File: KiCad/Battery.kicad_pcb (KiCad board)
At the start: 2 copper layers, 19 x 29 mm, 25 parts, among them J1 Connector, J2 USB-C, J3 DC, Q1 RN1701, Q2 BSS169, Q3 BSS169, U1 ESP32-WROOM-32, U2 FT231XQ

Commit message: Tidy up PCB
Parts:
- added D2: D, Diode_SMD:D_1206_3216Metric, F.Cu at (131.7, 115.4)
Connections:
- R5 pad 1: VBUS -> DC
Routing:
- net DC: track 40.7 -> 62.6 mm, vias 3 -> 4
- net VBUS: track 51.2 -> 37.0 mm
- net USB3.3: track 14.5 -> 16.0 mm
- net GND: track 148.1 -> 149.0 mm
- net IO1: track 10.1 -> 9.59 mm
- net Net-(Q2-Pad1): track 15.6 -> 15.1 mm
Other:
- board text added: "2021-05-22"
- board text added: "V2"
- board text removed: "2021-05-20"
- board text removed: "V3"

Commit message: Library update
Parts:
- removed Q2: BSS169, Package_TO_SOT_SMD:SOT-23
- removed R10: 10K, RevK:R_0603
- Q3: value BSS169 -> 2N7002
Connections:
- U1 pad 35: Net-(Q2-Pad1) -> O
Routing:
- net Net-(Q2-Pad1): track 15.1 -> 0.00 mm, vias 1 -> 0
- net O: track 9.10 -> 21.5 mm, vias 0 -> 1
- net VBUS: track 37.0 -> 34.0 mm
- net GND: track 149.0 -> 150.3 mm
- net USB3.3: track 16.0 -> 14.8 mm

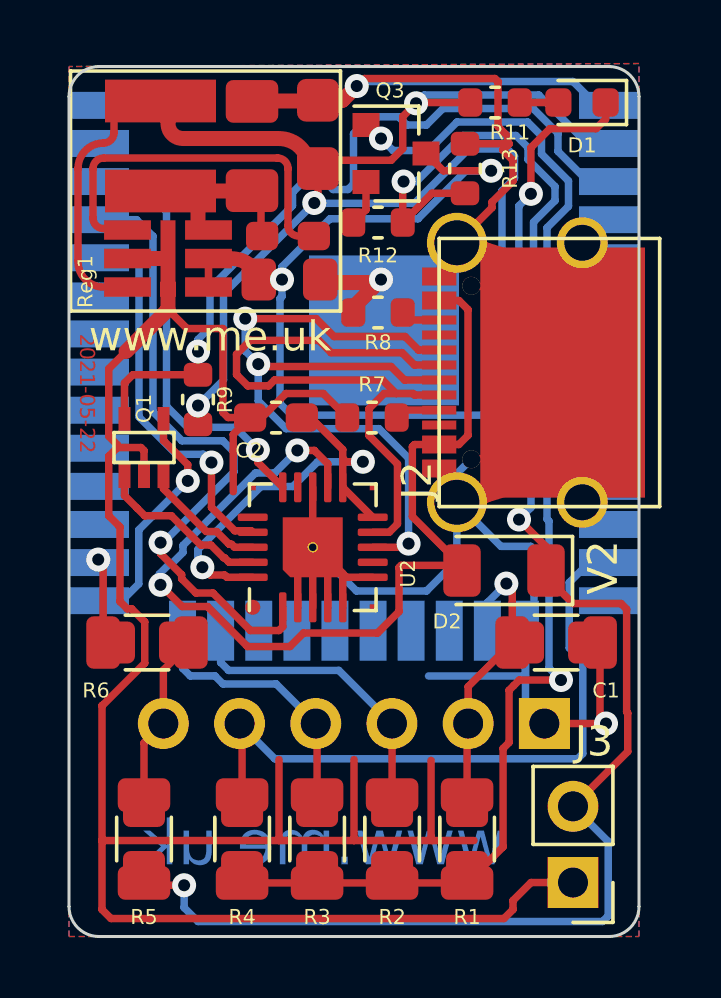
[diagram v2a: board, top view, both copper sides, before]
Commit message: Tidy, low current now
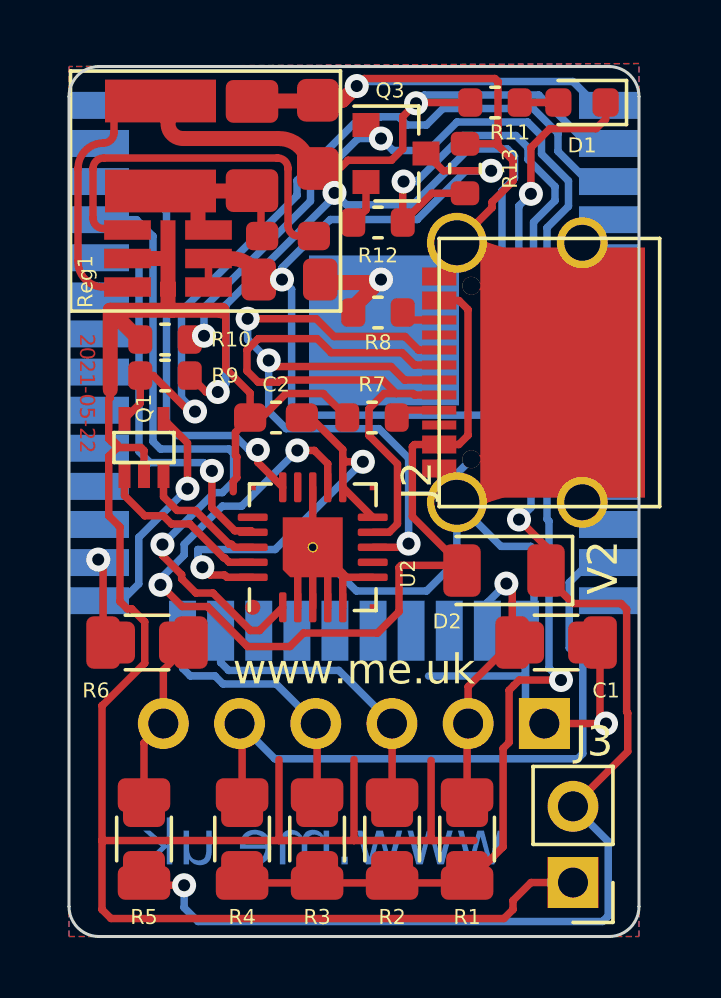
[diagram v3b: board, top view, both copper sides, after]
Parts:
- added R10: 10K, RevK:R_0603, F.Cu at (120.4, 107.7)
- moved R9 1.36 mm to (120.4, 108.9), turned to 0 degrees
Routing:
- net Net-(Q3-Pad1): track 16.9 -> 26.9 mm, vias 1 -> 2
- net GND: track 150.3 -> 152.9 mm
- net +3V3: track 66.5 -> 65.3 mm
- net Net-(Q1-Pad5): track 25.6 -> 26.5 mm
- net D-: track 21.5 -> 20.7 mm
- net I: track 12.9 -> 13.4 mm

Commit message: Fixed circuit
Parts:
- removed Q3: 2N7002, Package_TO_SOT_SMD:SOT-23
- added R14: 10K, RevK:R_0603, F.Cu at (134.9, 101.9)
- added U3: SSM6L14FE, Package_TO_SOT_SMD:SOT-563, F.Cu at (132.5, 101.8)
- moved R13 2.90 mm to (127.5, 101.9)
- moved R12 2.25 mm to (128.7, 101.9), turned to 270 degrees
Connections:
- net Net-(Q3-Pad1) renamed ADCON
- net Net-(R12-Pad2) renamed ADC
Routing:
- net ADC: track 19.9 -> 15.7 mm
- net DC: track 62.5 -> 66.5 mm
- net GND: track 152.9 -> 156.0 mm
- net Net-(R12-Pad1): track 1.53 -> 3.89 mm
- net Net-(R14-Pad1): track 0.00 -> 2.22 mm
- net +3V3: track 65.3 -> 63.4 mm
- net Net-(Q1-Pad5): track 26.5 -> 25.0 mm
- net ADCON: track 26.9 -> 25.5 mm
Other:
- net class 0.1 added: clearance 0.1, trace_width 0.25, via_dia 0.8, via_drill 0.4

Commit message: Tracked
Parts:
- U3: value SSM6L14FE -> NX6020CAKS; footprint Package_TO_SOT_SMD:SOT-563 -> Package_TO_SOT_SMD:SOT-23-6
- moved R11 2.53 mm to (128.9, 99.4)
- moved D1 0.64 mm to (134.7, 99.3)
- moved R14 0.40 mm to (135.3, 101.9), turned to 90 degrees
- moved U3 0.22 mm to (132.4, 102.0), turned to 270 degrees
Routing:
- net GND: track 156.0 -> 151.3 mm, vias 3 -> 4
- net Net-(D1-Pad2): track 1.29 -> 4.50 mm
- net Net-(D1-Pad1): track 15.9 -> 19.1 mm
- net ADCON: track 25.5 -> 28.3 mm
- net +3V3: track 63.4 -> 60.7 mm
- net Net-(R14-Pad1): track 2.22 -> 3.06 mm
- net Net-(Q1-Pad5): track 25.0 -> 25.7 mm
- net DC: track 66.5 -> 65.8 mm
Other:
- net class 0.1 removed

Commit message: Tweak
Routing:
- net GND: track 151.3 -> 154.3 mm
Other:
- board text added: "DC"

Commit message: Tweak
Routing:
- net DC: track 65.4 -> 66.2 mm

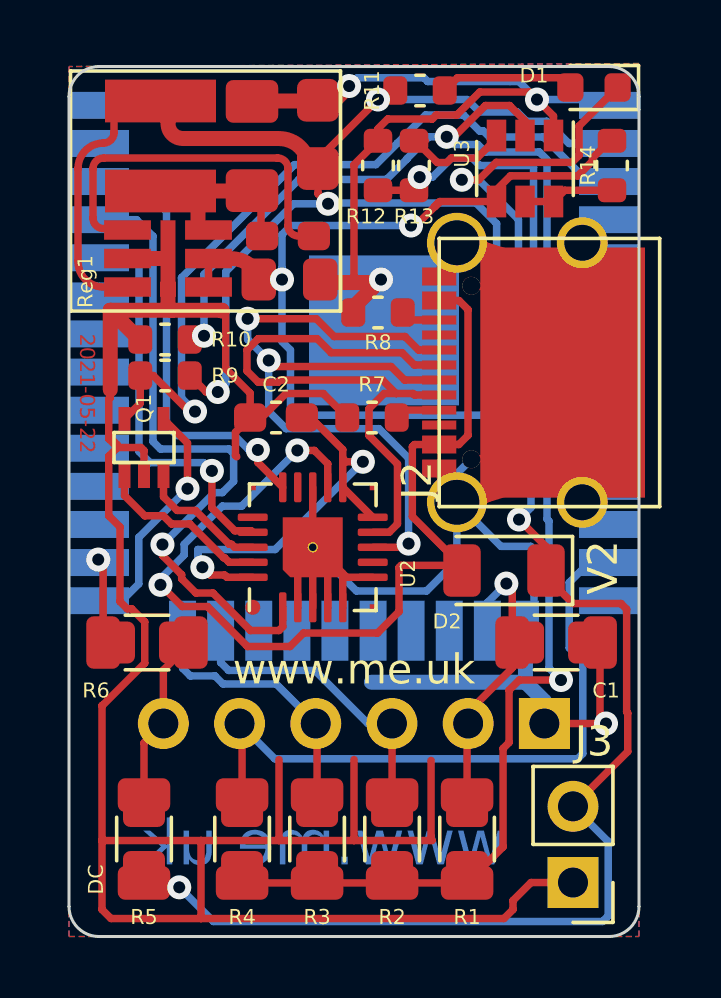
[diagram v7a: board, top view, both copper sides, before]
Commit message: New regulator
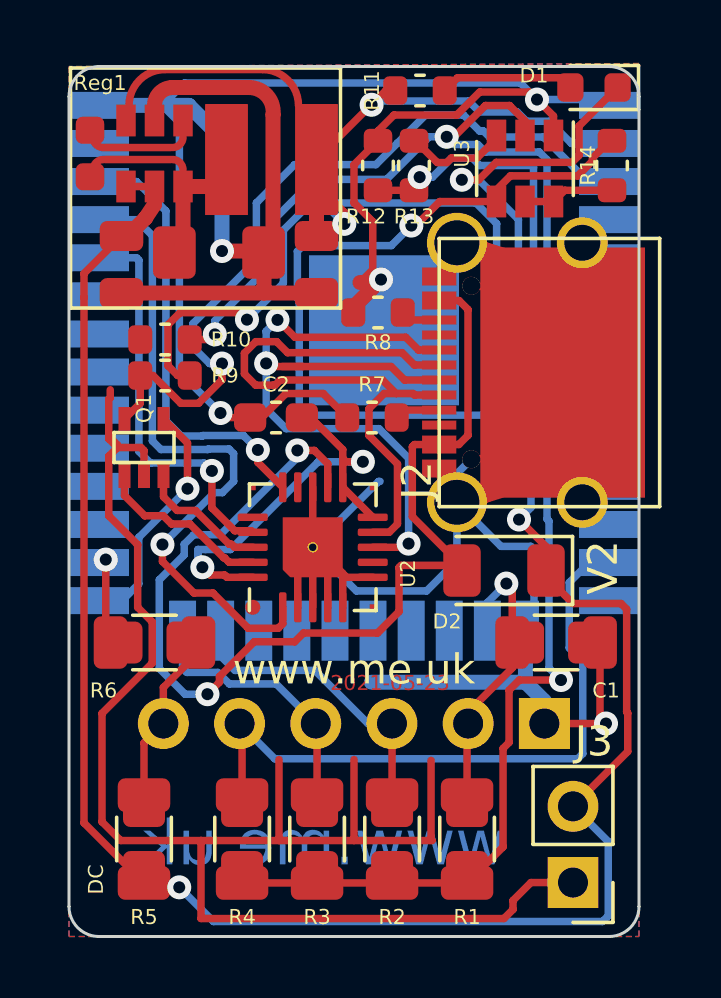
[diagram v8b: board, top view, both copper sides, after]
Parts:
- Reg1: footprint RevK:RegulatorBlock -> RevK:RegulatorBlock2
- moved Reg1 3.09 mm to (122.0, 102.3), turned to 0 degrees
- moved R6 0.25 mm to (120.0, 117.8)
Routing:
- net DC: track 66.2 -> 86.3 mm, vias 4 -> 3
- net GND: track 154.2 -> 165.9 mm, vias 4 -> 5
- net +3V3: track 61.2 -> 64.9 mm
- net VBUS: track 33.9 -> 37.2 mm
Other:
- board text added: "2021-05-23"
- board text removed: "2021-05-22"
